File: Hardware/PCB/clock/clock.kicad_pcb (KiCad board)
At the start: 2 copper layers, 9 parts, among them J1 Synth_power_2x5

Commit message: Initial layout, README update, software cleanup
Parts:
- removed the D2 at (178.9, 213.9)
- added C1: 100nF, ao_tht:C_Disc_D3.0mm_W1.6mm_P2.50mm, B.Cu at (160.0, 66.0)
- added C3: 100nF, ao_tht:C_Disc_D3.0mm_W1.6mm_P2.50mm, B.Cu at (200.7, 71.1)
- added D1: 1N4148, ao_tht:D_DO-35_SOD27_P7.62mm_Horizontal, B.Cu at (59.7, 114.3)
- added D3: LED_green, ao_tht:LED_D5.0mm, F.Cu at (78.7, 130.0)
- added D4: LED_green, ao_tht:LED_D5.0mm, F.Cu at (78.7, 145.0)
- added D5: LED_green, ao_tht:LED_D5.0mm, F.Cu at (78.7, 155.0)
- added D6: LED_green, ao_tht:LED_D5.0mm, F.Cu at (78.7, 170.0)
- added D7: LED_green, ao_tht:LED_D5.0mm, F.Cu at (78.7, 180.0)
- added GRAF2: Behind, clock:clock_panel_behind, F.Cu at (180.0, 100.0)
- added H1: MountingHole, ao_tht:MountingHole_3.2mm_M3, F.Cu at (200.0, 57.5)
- added H2: MountingHole, ao_tht:MountingHole_3.2mm_M3, B.Cu at (100.0, 57.5)
- added H3: MountingHole, ao_tht:MountingHole_3.2mm_M3, F.Cu at (159.7, 83.8)
- added H4: MountingHole, ao_tht:MountingHole_3.2mm_M3, B.Cu at (59.7, 83.8)
- added J1: AudioJack2, ao_tht:Jack_6.35mm_PJ_629HAN_slots, F.Cu at (67.5, 125.0)
- added J3: AudioJack2, ao_tht:Jack_6.35mm_PJ_629HAN_slots, F.Cu at (92.5, 125.0)
- added J4: AudioJack2, ao_tht:Jack_6.35mm_PJ_629HAN_slots, F.Cu at (67.5, 150.0)
- added J5: AudioJack2, ao_tht:Jack_6.35mm_PJ_629HAN_slots, F.Cu at (92.5, 150.0)
- added J6: AudioJack2, ao_tht:Jack_6.35mm_PJ_629HAN_slots, F.Cu at (67.5, 175.0)
- added J7: AudioJack2, ao_tht:Jack_6.35mm_PJ_629HAN_slots, F.Cu at (92.5, 175.0)
- added J8: Conn_02x04_Odd_Even, Connector_IDC:IDC-Header_2x04_P2.54mm_Vertical, B.Cu at (64.8, 69.8)
- added J9: Conn_02x04_Odd_Even, Connector_IDC:IDC-Header_2x04_P2.54mm_Vertical, B.Cu at (164.8, 49.5)
- added OLED1: OLED_128X64, Connector_PinHeader_2.54mm:PinHeader_1x04_P2.54mm_Vertical, F.Cu at (176.3, 17.1)
- added Q1: 2N3904, ao_tht:TO-92_Inline_Wide, B.Cu at (66.0, 106.7)
- added R1: 100k, ao_tht:R_Axial_DIN0204_L3.6mm_D1.6mm_P7.62mm_Horizontal, B.Cu at (69.8, 114.3)
- added R10: 10k, ao_tht:R_Axial_DIN0204_L3.6mm_D1.6mm_P7.62mm_Horizontal, B.Cu at (191.8, 96.5)
- added R11: 10k, ao_tht:R_Axial_DIN0204_L3.6mm_D1.6mm_P7.62mm_Horizontal, B.Cu at (69.8, 106.7)
- added R12: RL, ao_tht:R_Axial_DIN0204_L3.6mm_D1.6mm_P7.62mm_Horizontal, B.Cu at (81.3, 114.3)
- added R13: RL, ao_tht:R_Axial_DIN0204_L3.6mm_D1.6mm_P7.62mm_Horizontal, B.Cu at (78.7, 138.4)
- added R14: RL, ao_tht:R_Axial_DIN0204_L3.6mm_D1.6mm_P7.62mm_Horizontal, B.Cu at (81.3, 138.4)
- added R15: RL, ao_tht:R_Axial_DIN0204_L3.6mm_D1.6mm_P7.62mm_Horizontal, B.Cu at (78.7, 163.8)
- added R16: RL, ao_tht:R_Axial_DIN0204_L3.6mm_D1.6mm_P7.62mm_Horizontal, B.Cu at (81.3, 163.8)
- added R17: 1k, ao_tht:R_Axial_DIN0204_L3.6mm_D1.6mm_P7.62mm_Horizontal, B.Cu at (92.7, 114.3)
- added R18: 1k, ao_tht:R_Axial_DIN0204_L3.6mm_D1.6mm_P7.62mm_Horizontal, B.Cu at (67.3, 138.4)
- added R19: 1k, ao_tht:R_Axial_DIN0204_L3.6mm_D1.6mm_P7.62mm_Horizontal, B.Cu at (92.7, 138.4)
- added R2: 10k, ao_tht:R_Axial_DIN0204_L3.6mm_D1.6mm_P7.62mm_Horizontal, B.Cu at (160.0, 58.4)
- added R20: 1k, ao_tht:R_Axial_DIN0204_L3.6mm_D1.6mm_P7.62mm_Horizontal, B.Cu at (67.3, 163.8)
- added R21: 1k, ao_tht:R_Axial_DIN0204_L3.6mm_D1.6mm_P7.62mm_Horizontal, B.Cu at (92.7, 163.8)
- added R3: 10k, ao_tht:R_Axial_DIN0204_L3.6mm_D1.6mm_P7.62mm_Horizontal, B.Cu at (160.0, 69.8)
- added R4: 10k, ao_tht:R_Axial_DIN0204_L3.6mm_D1.6mm_P7.62mm_Horizontal, B.Cu at (200.7, 63.5)
- added R5: 10k, ao_tht:R_Axial_DIN0204_L3.6mm_D1.6mm_P7.62mm_Horizontal, B.Cu at (199.4, 92.7)
- added R6: 1M, ao_tht:R_Axial_DIN0204_L3.6mm_D1.6mm_P7.62mm_Horizontal, B.Cu at (69.8, 110.5)
- added R7: 10k, ao_tht:R_Axial_DIN0204_L3.6mm_D1.6mm_P7.62mm_Horizontal, B.Cu at (167.6, 62.2)
- added R8: 10k, ao_tht:R_Axial_DIN0204_L3.6mm_D1.6mm_P7.62mm_Horizontal, B.Cu at (167.6, 73.7)
- added R9: 10k, ao_tht:R_Axial_DIN0204_L3.6mm_D1.6mm_P7.62mm_Horizontal, B.Cu at (193.0, 67.3)
- added SW1: RotaryEncoder, ao_tht:RotaryEncoder_Bourns-PEC11R-4xxxF-Sxxxx-Switch_Vertical_H20mm, F.Cu at (172.5, 62.5)
- added SW2: SW_Push, ao_tht:Tactile_E-switch_TL1100F160Q, F.Cu at (180.0, 95.0)
- added TP1: +12V, ao_tht:TestPoint_THTPad_D1.5mm_Drill0.7mm, B.Cu at (101.6, 104.1)
- added TP2: GND, ao_tht:TestPoint_THTPad_D1.5mm_Drill0.7mm, B.Cu at (101.6, 97.8)
- added TP3: +5V, ao_tht:TestPoint_THTPad_D1.5mm_Drill0.7mm, B.Cu at (101.6, 91.4)
- added U1: 40106, ao_tht:DIP-14_W7.62mm_Socket_LongPads, B.Cu at (66.0, 99.1)
- A1: footprint ao_tht:Arduino_Nano -> Module:Arduino_Nano; moved to B.Cu
- C2: value 10uF -> 100nF; footprint ao_tht:CP_Radial_D6.3mm_P2.50mm -> ao_tht:C_Disc_D3.0mm_W1.6mm_P2.50mm; moved to B.Cu
- C4: moved to B.Cu
- C5: renamed from C1; moved to B.Cu
- C6: renamed from C3; moved to B.Cu
- D2: renamed from D1; moved to B.Cu
- GRAF1: value Graphic -> Holes; footprint clock:clock_panel_mockup -> clock:clock_panel_holes
- J2: renamed from J1; moved to B.Cu
- moved C6 162.4 mm to (77.5, 102.9), turned to 180 degrees
- moved C5 162.0 mm to (88.9, 57.1), turned to 180 degrees
- moved D2 138.1 mm to (100.3, 73.7), turned to 90 degrees
- moved J2 127.9 mm to (95.2, 49.5), turned to 90 degrees
- moved C2 79.0 mm to (160.0, 77.5)
- moved A1 48.1 mm to (81.3, 104.1), turned to 0 degrees
- moved C4 41.0 mm to (199.4, 100.3), turned to 180 degrees
- moved GRAF1 20.0 mm to (80.0, 100.0)
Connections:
- net -12V renamed GND1
- net /-12_IN renamed Net-(J2-Pad1)
- A1 pad 1: Net-(A1-Pad1) -> unconnected-(A1-Pad1)
- A1 pad 10: Net-(A1-Pad10) -> /ENC_A
- A1 pad 11: Net-(A1-Pad11) -> /ENC_B
- A1 pad 12: Net-(A1-Pad12) -> /ENC_PUSH
- A1 pad 13: Net-(A1-Pad13) -> /TACT
- A1 pad 14: Net-(A1-Pad14) -> /CLOCK_IN
- A1 pad 15: Net-(A1-Pad15) -> unconnected-(A1-Pad15)
- A1 pad 16: Net-(A1-Pad16) -> unconnected-(A1-Pad16)
- A1 pad 17: Net-(A1-Pad17) -> unconnected-(A1-Pad17)
- A1 pad 18: Net-(A1-Pad18) -> unconnected-(A1-Pad18)
- A1 pad 19: Net-(A1-Pad19) -> unconnected-(A1-Pad19)
- A1 pad 2: Net-(A1-Pad2) -> unconnected-(A1-Pad2)
- A1 pad 20: Net-(A1-Pad20) -> unconnected-(A1-Pad20)
- A1 pad 21: Net-(A1-Pad21) -> unconnected-(A1-Pad21)
- A1 pad 22: Net-(A1-Pad22) -> unconnected-(A1-Pad22)
- A1 pad 23: Net-(A1-Pad23) -> /SCA
- A1 pad 24: Net-(A1-Pad24) -> /SCL
- A1 pad 25: Net-(A1-Pad25) -> unconnected-(A1-Pad25)
- A1 pad 26: Net-(A1-Pad26) -> unconnected-(A1-Pad26)
- A1 pad 27: Net-(A1-Pad27) -> +5V
- A1 pad 28: Net-(A1-Pad28) -> unconnected-(A1-Pad28)
- A1 pad 29: Net-(A1-Pad29) -> GND
- A1 pad 3: Net-(A1-Pad3) -> unconnected-(A1-Pad3)
- A1 pad 30: Net-(A1-Pad30) -> +12V
- A1 pad 4: Net-(A1-Pad4) -> GND
- A1 pad 5: Net-(A1-Pad5) -> /CLOCK_OUT
- A1 pad 6: Net-(A1-Pad6) -> /DIV_2
- A1 pad 7: Net-(A1-Pad7) -> /DIV_4
- A1 pad 8: Net-(A1-Pad8) -> /DIV_8
- A1 pad 9: Net-(A1-Pad9) -> /DIV_N
- C2 pad 1: GND -> /ENC_B_JA
- C4 pad 1: GND -> /TACT_JA
- C6 pad 1: +12V -> +5V
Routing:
- net +5V_1: track 0.00 -> 133.7 mm
- net /DIV_N: track 0.00 -> 92.3 mm
- net /DIV_8: track 0.00 -> 87.5 mm
- net +5V: track 0.00 -> 86.8 mm
- net +12V: track 0.00 -> 69.3 mm
- net /TACT_JA: track 0.00 -> 66.4 mm
- net /DIV_4: track 0.00 -> 59.4 mm
- net /DIV_2: track 0.00 -> 56.0 mm
- net /SCL: track 0.00 -> 44.3 mm
- net /ENC_PUSH_JA: track 0.00 -> 43.5 mm
- net /SCA: track 0.00 -> 39.0 mm
- net /SCL_JA: track 0.00 -> 37.2 mm
- net /SCA_JA: track 0.00 -> 37.2 mm
- net Net-(Q1-Pad3): track 0.00 -> 36.1 mm
- net /ENC_B_JA: track 0.00 -> 29.5 mm
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- added copper zone on B.Cu, net GND
- added copper zone on F.Cu, net GND
- added copper zone on B.Cu, net GND1
- added copper zone on F.Cu, net GND1
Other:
- board outline added: 146 x 170.5 mm
- net class Default removed
- net class Power removed

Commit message: Layout revisions
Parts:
- GRAF2: footprint clock:clock_panel_behind -> clock:clock_panel_holes
- OLED1: footprint Connector_PinHeader_2.54mm:PinHeader_1x04_P2.54mm_Vertical -> ao_tht:OLED_MC130GX
- moved R7 5.00 mm to (167.6, 67.2)
- moved C1 5.00 mm to (160.0, 71.0)
- moved C2 5.00 mm to (160.0, 82.5)
- moved H3 5.00 mm to (159.7, 88.8)
- moved H4 5.00 mm to (59.7, 88.8)
- moved J9 5.00 mm to (164.8, 54.5)
- moved R2 5.00 mm to (160.0, 63.4)
- moved R3 5.00 mm to (160.0, 74.8)
- moved R8 5.00 mm to (167.6, 78.7)
- moved SW2 5.00 mm to (180.0, 100.0)
- moved SW1 5.00 mm to (172.5, 67.5)
- moved OLED1 0.11 mm to (176.2, 17.2), turned to 0 degrees
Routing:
- net +5V_1: track 133.7 -> 143.6 mm
- net /TACT_JA: track 66.4 -> 57.6 mm
- net /SCA_JA: track 37.2 -> 42.1 mm
- net /SCL_JA: track 37.2 -> 42.1 mm
- net /ENC_PUSH_JA: track 43.5 -> 42.4 mm
- net /ENC_A_JA: track 25.6 -> 26.5 mm
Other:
- outline, holes or cut-outs redrawn

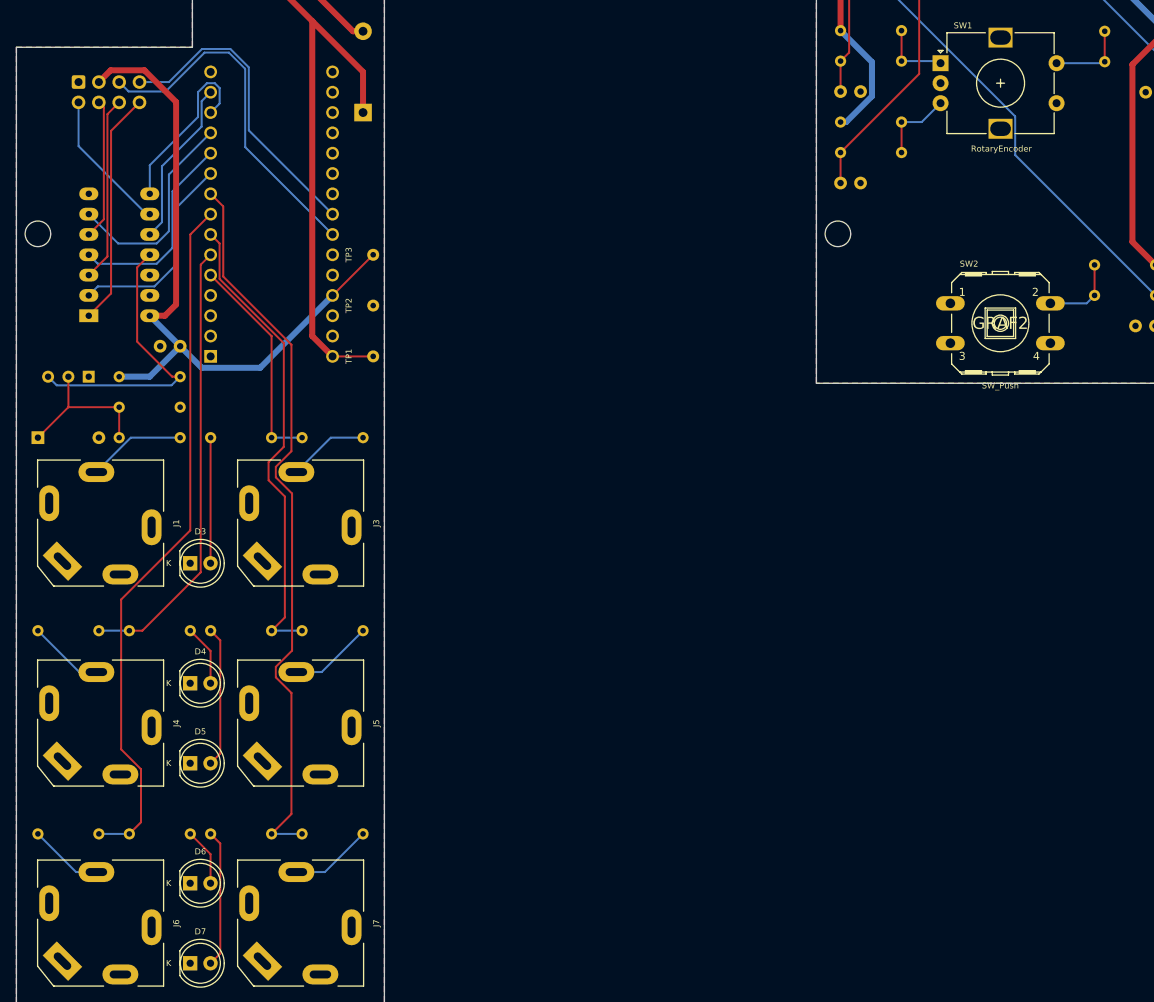
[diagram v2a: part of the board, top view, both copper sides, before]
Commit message: Add Zeners, reallocate XORs
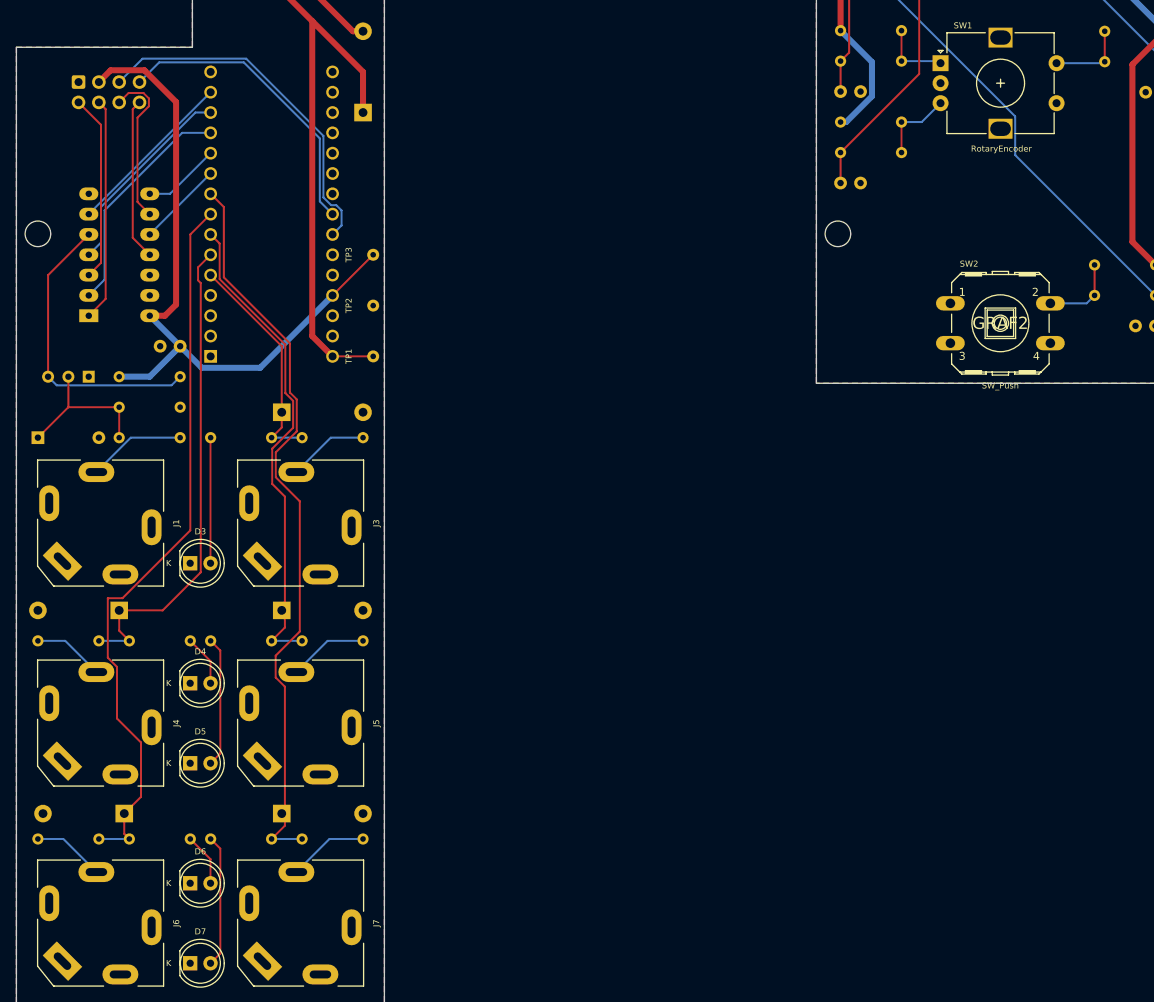
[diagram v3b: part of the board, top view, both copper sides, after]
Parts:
- added D10: 1N4733A, ao_tht:D_DO-41_SOD81_P10.16mm_Horizontal, B.Cu at (90.2, 135.9)
- added D11: 1N4733A, ao_tht:D_DO-41_SOD81_P10.16mm_Horizontal, B.Cu at (70.5, 161.3)
- added D12: 1N4733A, ao_tht:D_DO-41_SOD81_P10.16mm_Horizontal, B.Cu at (90.2, 161.3)
- added D8: 1N4733A, ao_tht:D_DO-41_SOD81_P10.16mm_Horizontal, B.Cu at (90.2, 111.1)
- added D9: 1N4733A, ao_tht:D_DO-41_SOD81_P10.16mm_Horizontal, B.Cu at (69.8, 135.9)
- moved R13 1.27 mm to (78.7, 139.7)
- moved R14 1.27 mm to (81.3, 139.7)
- moved R18 1.27 mm to (67.3, 139.7)
- moved R19 1.27 mm to (92.7, 139.7)
- moved R15 0.63 mm to (78.7, 164.5)
- moved R16 0.63 mm to (81.3, 164.5)
- moved R20 0.63 mm to (67.3, 164.5)
- moved R21 0.63 mm to (92.7, 164.5)
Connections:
- U1 pad 1: /ENC_A_JB -> /ENC_PUSH_JB
- U1 pad 10: /CLOCK_IN -> /ENC_A
- U1 pad 11: Net-(Q1-Pad3) -> /ENC_A_JB
- U1 pad 2: /ENC_A -> /ENC_PUSH
- U1 pad 3: /ENC_B_JB -> /TACT_JB
- U1 pad 4: /ENC_B -> /TACT
- U1 pad 5: /ENC_PUSH_JB -> Net-(Q1-Pad3)
- U1 pad 6: /ENC_PUSH -> /CLOCK_IN
- U1 pad 8: /TACT -> /ENC_B
- U1 pad 9: /TACT_JB -> /ENC_B_JB
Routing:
- net /ENC_B: track 25.6 -> 9.71 mm
- net /ENC_A: track 25.7 -> 10.8 mm
- net /ENC_PUSH_JB: track 17.5 -> 27.9 mm
- net /ENC_A_JB: track 29.3 -> 20.3 mm
- net /TACT_JB: track 17.9 -> 23.4 mm
- net /DIV_2: track 56.0 -> 60.8 mm
- net /DIV_8: track 87.5 -> 91.2 mm
- net /TACT: track 22.2 -> 25.2 mm
- net /ENC_B_JB: track 23.2 -> 20.2 mm
- net /ENC_PUSH: track 26.6 -> 28.7 mm
- net /DIV_4: track 59.4 -> 61.3 mm
- net /SCA: track 39.0 -> 37.6 mm
- net /DIV_N: track 92.3 -> 93.7 mm
- net /DIV_4_L: track 17.6 -> 16.3 mm
- net /DIV_2_L: track 7.62 -> 6.35 mm
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
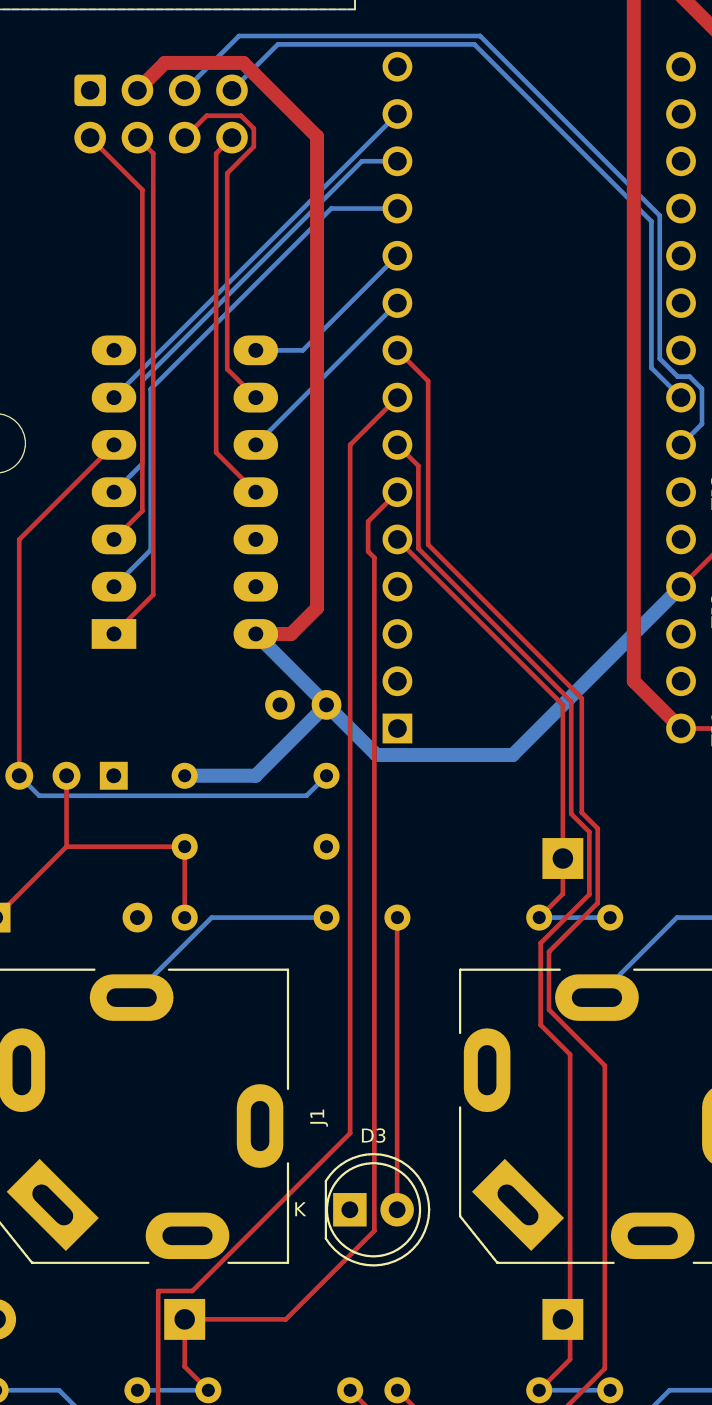
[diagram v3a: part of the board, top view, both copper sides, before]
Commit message: Rearrange digital pins (for encoder to interrupt pin 2)
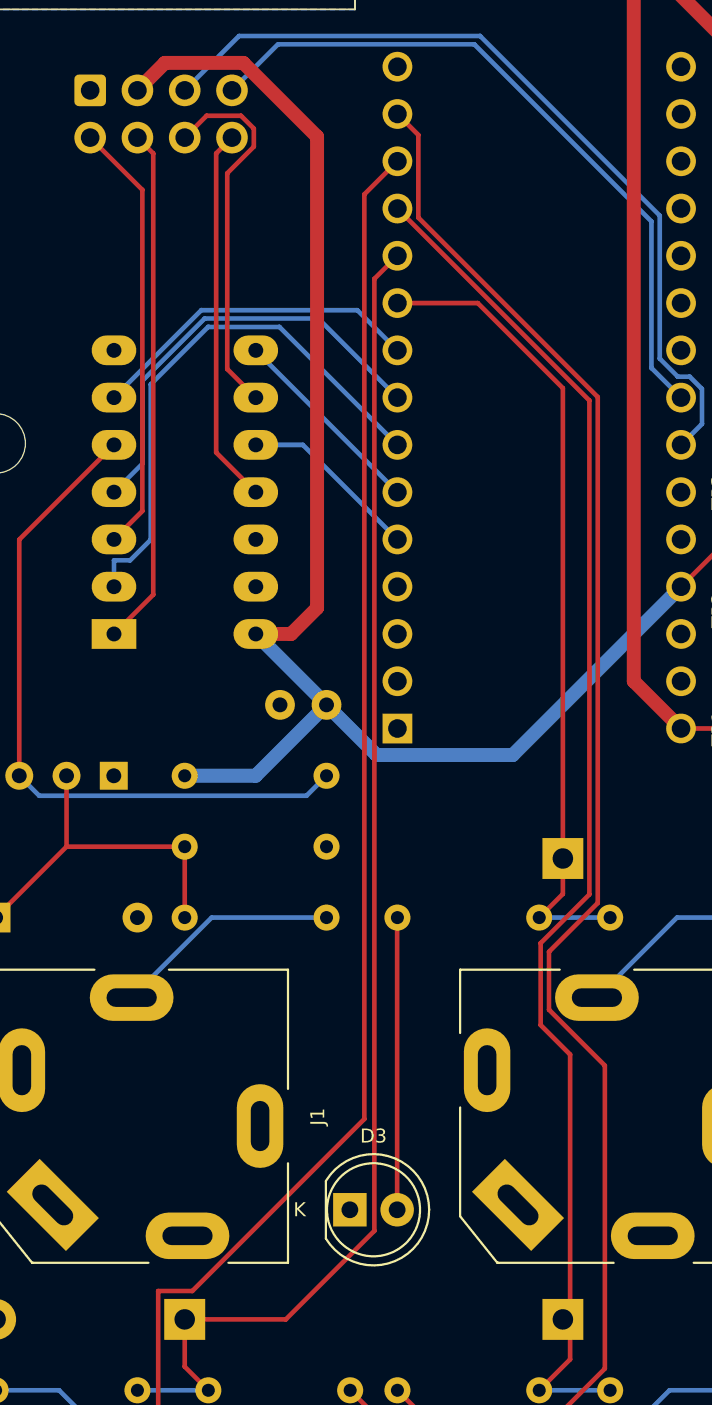
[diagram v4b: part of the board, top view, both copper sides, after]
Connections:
- A1 pad 10: /ENC_A -> /CLOCK_OUT
- A1 pad 11: /ENC_B -> /DIV_2
- A1 pad 12: /ENC_PUSH -> /DIV_4
- A1 pad 13: /TACT -> /DIV_8
- A1 pad 14: /CLOCK_IN -> /DIV_N
- A1 pad 5: /CLOCK_OUT -> /ENC_A
- A1 pad 6: /DIV_2 -> /ENC_B
- A1 pad 7: /DIV_4 -> /ENC_PUSH
- A1 pad 8: /DIV_8 -> /TACT
- A1 pad 9: /DIV_N -> /CLOCK_IN
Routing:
- net /CLOCK_OUT: track 28.3 -> 43.6 mm
- net /DIV_8: track 91.2 -> 103.9 mm
- net /DIV_4: track 61.3 -> 74.0 mm
- net /DIV_N: track 93.7 -> 106.4 mm
- net /DIV_2: track 60.8 -> 73.2 mm
- net /CLOCK_IN: track 21.5 -> 18.1 mm
- net /TACT: track 25.2 -> 23.5 mm
- net /ENC_B: track 9.71 -> 10.8 mm
- net /ENC_A: track 10.8 -> 9.72 mm
- net /ENC_PUSH: track 28.7 -> 29.4 mm
